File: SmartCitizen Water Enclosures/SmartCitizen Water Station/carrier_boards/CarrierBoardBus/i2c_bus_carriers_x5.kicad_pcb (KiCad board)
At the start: 2 copper layers, 96 x 18 mm, 6 parts, among them J1 Conn_PinHeader_1x05_P2.54mm_V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, J2 Conn_PinHeader_1x05_P2.54mm_V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, J3 Conn_PinHeader_1x05_P2.54mm_V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, J4 Conn_PinHeader_1x05_P2.54mm_V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, J5 Conn_PinHeader_1x05_P2.54mm_V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, J6 GROVE-CONNECTOR-SMD-90D_4+2P-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

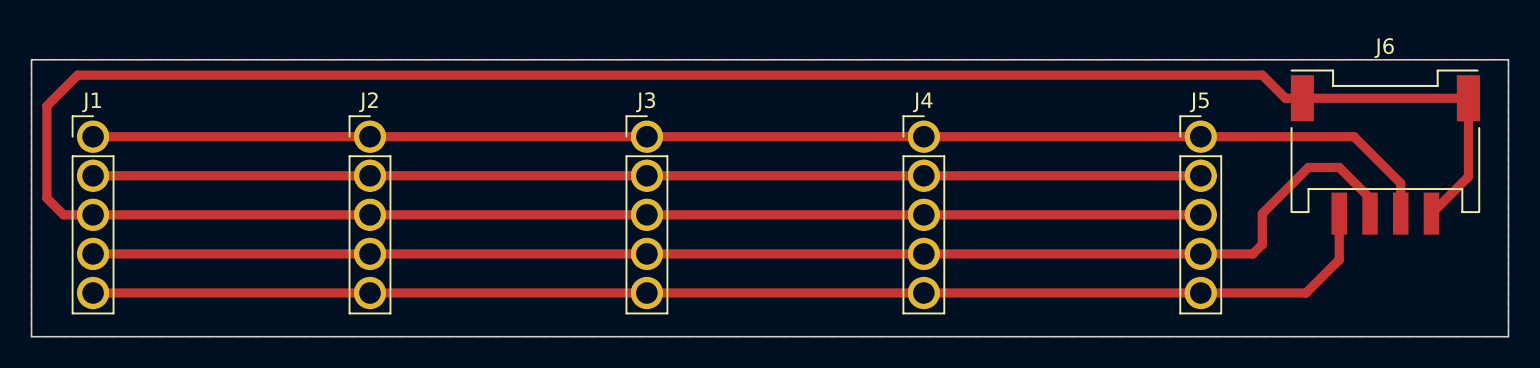
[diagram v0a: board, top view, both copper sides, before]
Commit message: Add silkscreen to carrier boards
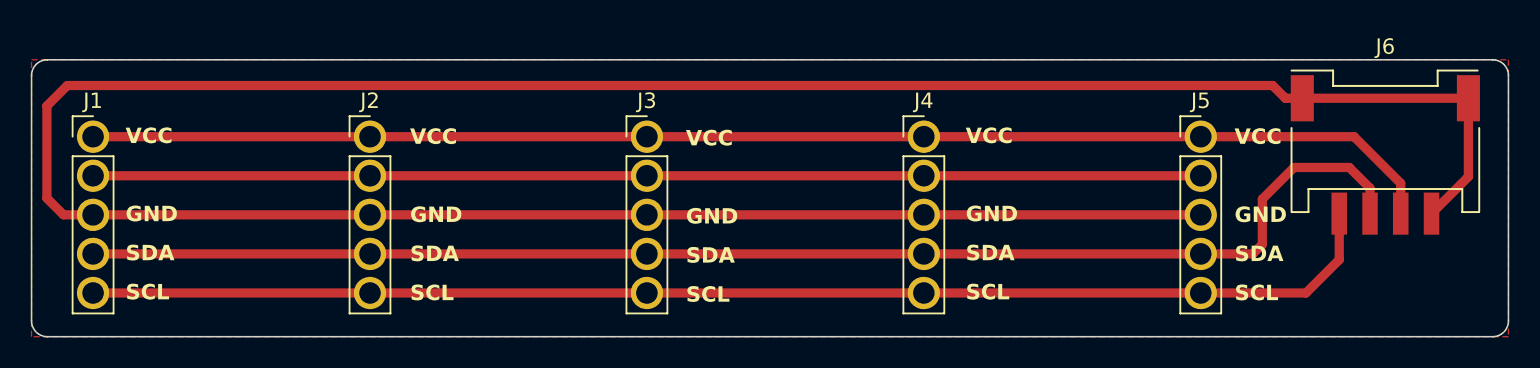
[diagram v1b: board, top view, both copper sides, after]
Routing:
- net sda: track 88.3 -> 89.3 mm
- net GND: track 183.8 -> 183.2 mm
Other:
- outline, holes or cut-outs redrawn
- board text added: "GND"
- board text added: "SCL"
- board text added: "SDA"
- board text added: "Smart Citizen OHL Use with caution"
- board text added: "THIS SIDE UP!"
- board text added: "VCC"
- board text added: "VCC LINE"
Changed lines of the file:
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@@
     )
     (pad_to_mask_clearance 0)
+    (grid_origin 140.6652 52.324)
     (pcbplotparams
       (layerselection 0x00010fc_ffffffff)
@@
       (outputformat 1)
       (mirror false)
-      (drillshape 1)
+      (drillshape 0)
       (scaleselection 1)
-      (outputdirectory "")
+      (outputdirectory "exports/")
     )
   )
@@
       (net 3 "GND") (pinfunction "SS2") (pintype "bidirectional"))
   )
-  (gr_rect (start 96 57) (end 192 75)
-    (stroke (width 0.1) (type default)) (fill none) (layer "Edge.Cuts"))
+  (gr_line (start 98.3488 59.3852) (end 98.9076 59.944)
+    (stroke (width 0.8) (type default)) (layer "B.SilkS"))
+  (gr_line (start 188.2648 58.928) (end 189.3316 59.9948)
+    (stroke (width 0.8) (type default)) (layer "B.SilkS"))
+  (gr_line (start 162.5092 59.3852) (end 98.3488 59.3852)
+    (stroke (width 0.8) (type default)) (layer "B.SilkS"))
+  (gr_line (start 180.5432 61.722) (end 180.5432 58.8772)
+    (stroke (width 0.8) (type default)) (layer "B.SilkS"))
+  (gr_line (start 179.4764 59.944) (end 180.5432 58.8772)
+    (stroke (width 0.8) (type default)) (layer "B.SilkS"))
+  (gr_line (start 177.419 58.166) (end 190.5762 58.166)
+    (stroke (width 0.15) (type default)) (layer "B.SilkS"))
+  (gr_line (start 188.2648 61.7728) (end 188.2648 58.928)
+    (stroke (width 0.8) (type default)) (layer "B.SilkS"))
+  (gr_line (start 180.5432 58.8772) (end 181.61 59.944)
+    (stroke (width 0.8) (type default)) (layer "B.SilkS"))
+  (gr_line (start 187.198 59.9948) (end 188.2648 58.928)
+    (stroke (width 0.8) (type default)) (layer "B.SilkS"))
+  (gr_line (start 98.9076 58.8264) (end 98.3488 59.3852)
+    (stroke (width 0.8) (type default)) (layer "B.SilkS"))
+  (gr_line (start 98.3488 59.3852) (end 98.9076 58.8264)
+    (stroke (width 0.8) (type default)) (layer "B.SilkS"))
+  (gr_arc (start 96 58.028) (mid 96.301094 57.301094) (end 97.028 57)
+    (stroke (width 0.1) (type default)) (layer "Edge.Cuts"))
+  (gr_arc (start 190.972 57) (mid 191.698906 57.301094) (end 192 58.028)
+    (stroke (width 0.1) (type default)) (layer "Edge.Cuts"))
+  (gr_arc (start 97.028 75) (mid 96.301094 74.698906) (end 96 73.972)
+    (stroke (width 0.1) (type default)) (layer "Edge.Cuts"))
+  (gr_arc (start 192 73.972) (mid 191.698906 74.698906) (end 190.972 75)
+    (stroke (width 0.1) (type default)) (layer "Edge.Cuts"))
+  (gr_line (start 192 58.028) (end 192 73.972)
+    (stroke (width 0.1) (type default)) (layer "Edge.Cuts"))
+  (gr_line (start 190.972 75) (end 97.028 75)
+    (stroke (width 0.1) (type default)) (layer "Edge.Cuts"))
+  (gr_line (start 97.028 57) (end 190.972 57)
+    (stroke (width 0.1) (type default)) (layer "Edge.Cuts"))
+  (gr_line (start 96 73.972) (end 96 58.028)
+    (stroke (width 0.1) (type default)) (layer "Edge.Cuts"))
+  (gr_text "THIS SIDE UP!" (at 189.738 63.6524) (layer "B.SilkS")
+    (effects (font (size 1 1) (thickness 0.2) bold) (justify left bottom mirror))
+  )
+  (gr_text "VCC LINE" (at 170.2308 60.0964) (layer "B.SilkS")
+    (effects (font (size 1 1) (thickness 0.2) bold) (justify left bottom mirror))
+  )
+  (gr_text "Smart Citizen\nOHL\nUse with caution" (at 189.8904 71.882) (layer "B.SilkS")
+    (effects (font (size 1 1) (thickness 0.2) bold) (justify left bottom mirror))
+  )
+  (gr_text "GND" (at 120.5992 67.6656) (layer "F.SilkS")
+    (effects (font (size 1 1) (thickness 0.2) bold) (justify left bottom))
+  )
+  (gr_text "SCL" (at 102.108 72.6948) (layer "F.SilkS")
+    (effects (font (size 1 1) (thickness 0.2) bold) (justify left bottom))
+  )
+  (gr_text "SCL" (at 138.5316 72.8472) (layer "F.SilkS")
+    (effects (font (size 1 1) (thickness 0.2) bold) (justify left bottom))
+  )
+  (gr_text "SCL" (at 156.718 72.6948) (layer "F.SilkS")
+    (effects (font (size 1 1) (thickness 0.2) bold) (justify left bottom))
+  )
+  (gr_text "GND" (at 156.718 67.6148) (layer "F.SilkS")
+    (effects (font (size 1 1) (thickness 0.2) bold) (justify left bottom))
+  )
+  (gr_text "GND" (at 102.108 67.6148) (layer "F.SilkS")
+    (effects (font (size 1 1) (thickness 0.2) bold) (justify left bottom))
+  )
+  (gr_text "VCC" (at 120.5992 62.5856) (layer "F.SilkS")
+    (effects (font (size 1 1) (thickness 0.2) bold) (justify left bottom))
+  )
+  (gr_text "VCC" (at 102.108 62.5348) (layer "F.SilkS")
+    (effects (font (size 1 1) (thickness 0.2) bold) (justify left bottom))
+  )
+  (gr_text "SDA" (at 102.108 70.1548) (layer "F.SilkS")
+    (effects (font (size 1 1) (thickness 0.2) bold) (justify left bottom))
+  )
+  (gr_text "SDA" (at 156.718 70.1548) (layer "F.SilkS")
+    (effects (font (size 1 1) (thickness 0.2) bold) (justify left bottom))
+  )
+  (gr_text "GND" (at 138.5316 67.7672) (layer "F.SilkS")
+    (effects (font (size 1 1) (thickness 0.2) bold) (justify left bottom))
+  )
+  (gr_text "SDA" (at 120.5992 70.2056) (layer "F.SilkS")
+    (effects (font (size 1 1) (thickness 0.2) bold) (justify left bottom))
+  )
+  (gr_text "SDA" (at 174.1932 70.2056) (layer "F.SilkS")
+    (effects (font (size 1 1) (thickness 0.2) bold) (justify left bottom))
+  )
+  (gr_text "VCC" (at 138.5316 62.6872) (layer "F.SilkS")
+    (effects (font (size 1 1) (thickness 0.2) bold) (justify left bottom))
+  )
+  (gr_text "VCC" (at 156.718 62.5348) (layer "F.SilkS")
+    (effects (font (size 1 1) (thickness 0.2) bold) (justify left bottom))
+  )
+  (gr_text "GND" (at 174.1932 67.6656) (layer "F.SilkS")
+    (effects (font (size 1 1) (thickness 0.2) bold) (justify left bottom))
+  )
+  (gr_text "SCL" (at 120.5992 72.7456) (layer "F.SilkS")
+    (effects (font (size 1 1) (thickness 0.2) bold) (justify left bottom))
+  )
+  (gr_text "SCL" (at 174.1932 72.7456) (layer "F.SilkS")
+    (effects (font (size 1 1) (thickness 0.2) bold) (justify left bottom))
+  )
+  (gr_text "SDA" (at 138.5316 70.3072) (layer "F.SilkS")
+    (effects (font (size 1 1) (thickness 0.2) bold) (justify left bottom))
+  )
+  (gr_text "VCC" (at 174.1932 62.5856) (layer "F.SilkS")
+    (effects (font (size 1 1) (thickness 0.2) bold) (justify left bottom))
+  )
   (segment (start 118 62) (end 136 62) (width 0.6) (layer "F.Cu") (net 1))
   (segment (start 100 62) (end 118 62) (width 0.6) (layer "F.Cu") (net 1))
@@
   (segment (start 118 64.54) (end 136 64.54) (width 0.6) (layer "F.Cu") (net 2))
   (segment (start 100 64.54) (end 118 64.54) (width 0.6) (layer "F.Cu") (net 2))
-  (segment (start 98.08 67.08) (end 97 66) (width 0.6) (layer "F.Cu") (net 3))
   (segment (start 178.60224 59.50192) (end 189.39724 59.50192) (width 0.6) (layer "F.Cu") (net 3))
   (segment (start 118 67.08) (end 136 67.08) (width 0.6) (layer "F.Cu") (net 3))
-  (segment (start 177.50192 59.50192) (end 178.60224 59.50192) (width 0.6) (layer "F.Cu") (net 3))
-  (segment (start 100 67.08) (end 98.08 67.08) (width 0.6) (layer "F.Cu") (net 3))
   (segment (start 136 67.08) (end 154 67.08) (width 0.6) (layer "F.Cu") (net 3))
-  (segment (start 99 58) (end 176 58) (width 0.6) (layer "F.Cu") (net 3))
+  (segment (start 98.08 67.08) (end 97 66) (width 0.6) (layer "F.Cu") (net 3))
   (segment (start 189.39724 59.50192) (end 189.39724 64.60224) (width 0.6) (layer "F.Cu") (net 3))
+  (segment (start 97 60) (end 98.326 58.674) (width 0.6) (layer "F.Cu") (net 3))
   (segment (start 189.39724 64.60224) (end 186.99948 67) (width 0.6) (layer "F.Cu") (net 3))
   (segment (start 100 67.08) (end 118 67.08) (width 0.6) (layer "F.Cu") (net 3))
+  (segment (start 100 67.08) (end 98.08 67.08) (width 0.6) (layer "F.Cu") (net 3))
   (segment (start 154 67.08) (end 172 67.08) (width 0.6) (layer "F.Cu") (net 3))
+  (segment (start 177.50192 59.50192) (end 178.60224 59.50192) (width 0.6) (layer "F.Cu") (net 3))
+  (segment (start 176.674 58.674) (end 177.50192 59.50192) (width 0.6) (layer "F.Cu") (net 3))
   (segment (start 97 66) (end 97 60) (width 0.6) (layer "F.Cu") (net 3))
-  (segment (start 97 60) (end 99 58) (width 0.6) (layer "F.Cu") (net 3))
-  (segment (start 176 58) (end 177.50192 59.50192) (width 0.6) (layer "F.Cu") (net 3))
+  (segment (start 98.326 58.674) (end 176.674 58.674) (width 0.6) (layer "F.Cu") (net 3))
   (segment (start 154 69.62) (end 172 69.62) (width 0.6) (layer "F.Cu") (net 4))
-  (segment (start 181 64) (end 183.00152 66.00152) (width 0.6) (layer "F.Cu") (net 4))
-  (segment (start 179 64) (end 181 64) (width 0.6) (layer "F.Cu") (net 4))
+  (segment (start 183.00152 65.34872) (end 183.00152 67) (width 0.6) (layer "F.Cu") (net 4))
+  (segment (start 172 69.62) (end 175.38 69.62) (width 0.6) (layer "F.Cu") (net 4))
+  (segment (start 181.6528 64) (end 183.00152 65.34872) (width 0.6) (layer "F.Cu") (net 4))
   (segment (start 136 69.62) (end 154 69.62) (width 0.6) (layer "F.Cu") (net 4))
-  (segment (start 176 69) (end 176 67) (width 0.6) (layer "F.Cu") (net 4))
-  (segment (start 183.00152 66.00152) (end 183.00152 67) (width 0.6) (layer "F.Cu") (net 4))
-  (segment (start 172 69.62) (end 175.38 69.62) (width 0.6) (layer "F.Cu") (net 4))
+  (segment (start 176 69) (end 176 66.062) (width 0.6) (layer "F.Cu") (net 4))
   (segment (start 175.38 69.62) (end 176 69) (width 0.6) (layer "F.Cu") (net 4))
+  (segment (start 178.062 64) (end 181.6528 64) (width 0.6) (layer "F.Cu") (net 4))
   (segment (start 118 69.62) (end 136 69.62) (width 0.6) (layer "F.Cu") (net 4))
-  (segment (start 176 67) (end 179 64) (width 0.6) (layer "F.Cu") (net 4))
+  (segment (start 176 66.062) (end 178.062 64) (width 0.6) (layer "F.Cu") (net 4))
   (segment (start 100 69.62) (end 118 69.62) (width 0.6) (layer "F.Cu") (net 4))
   (segment (start 154 72.16) (end 172 72.16) (width 0.6) (layer "F.Cu") (net 5))
